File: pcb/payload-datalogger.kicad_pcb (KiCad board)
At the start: 2 copper layers, 43.5 x 41 mm, 42 parts, among them J1 2.54mm 01x02 header, J2 Conn_01x02, J3 Conn_01x02, J4 Conn_01x02, J5 Conn_01x02, SW2 PTS815, U1 XIAO-ESP32-C3-DIP, U2 NCP177AMX330TCG, U3 W25X40CLSN, U4 MCP96RL00T-E_MX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

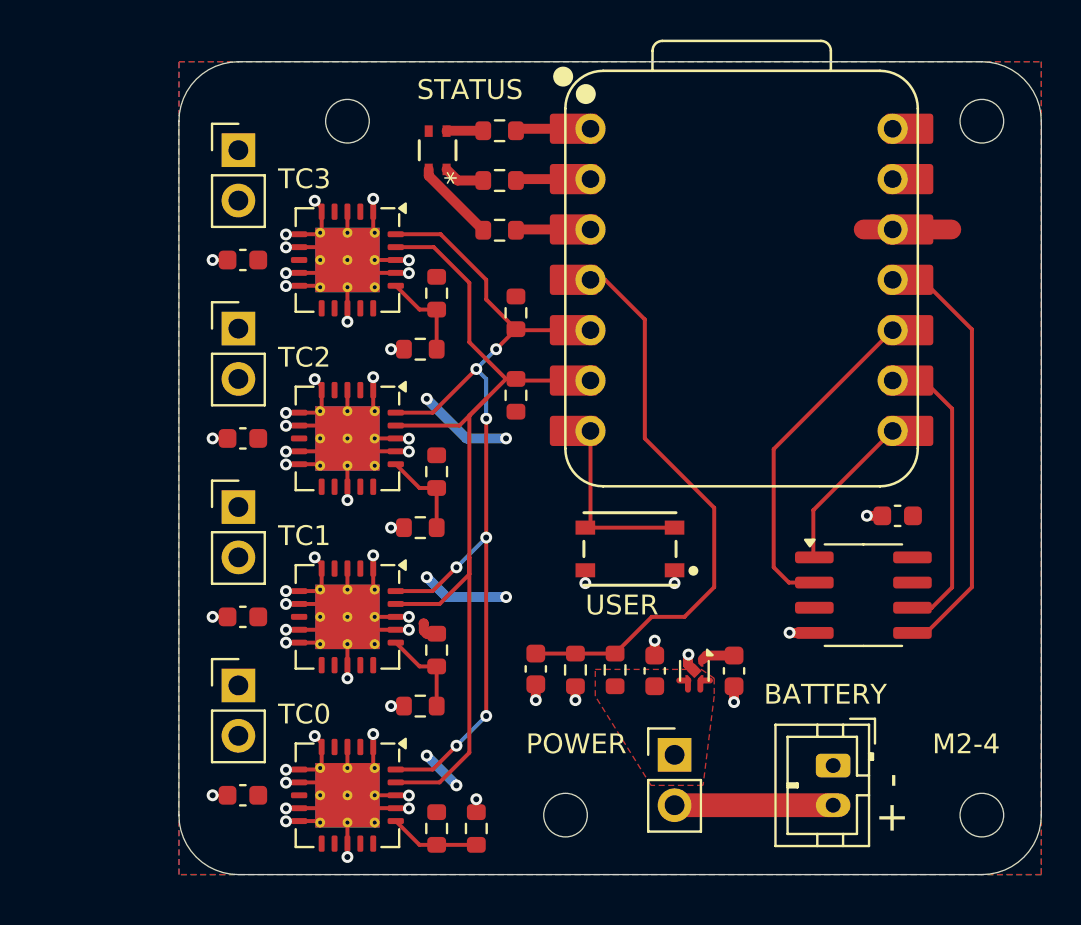
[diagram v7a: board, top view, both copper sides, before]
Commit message: Update PCB to use d sub
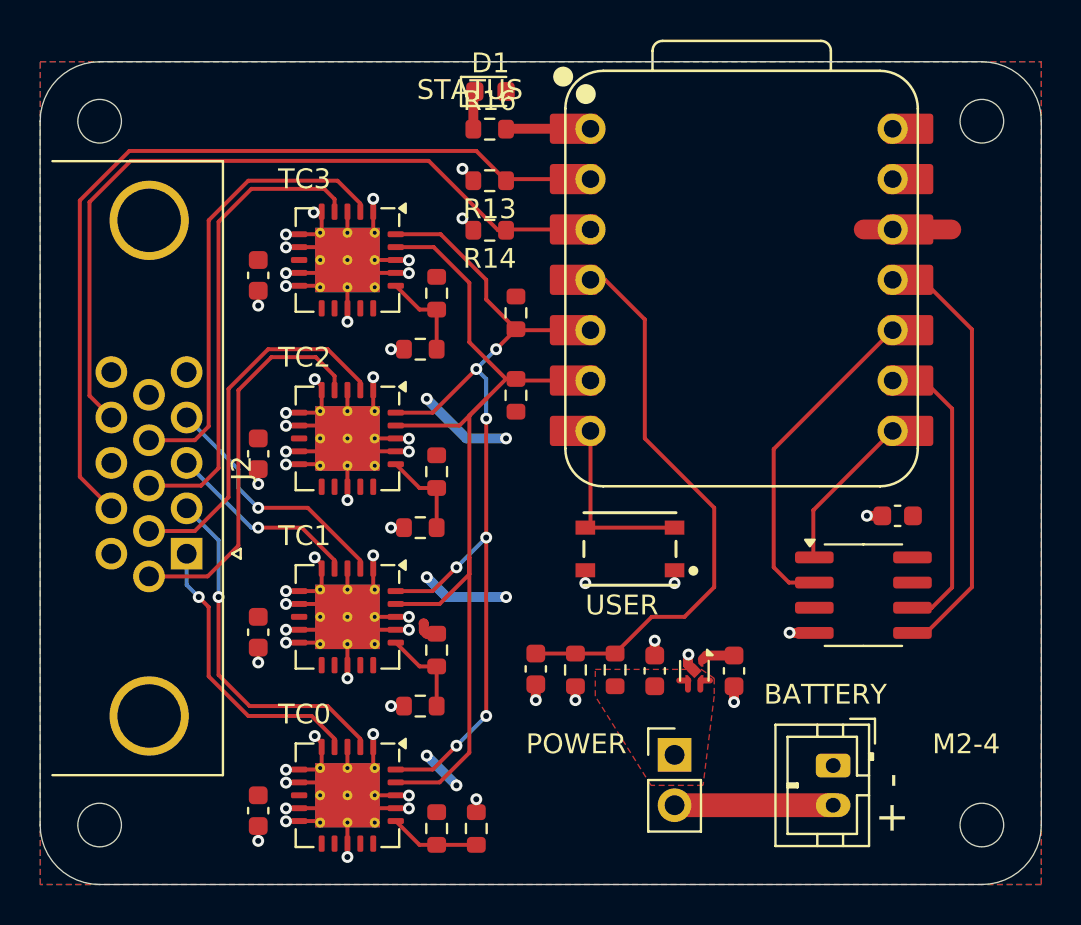
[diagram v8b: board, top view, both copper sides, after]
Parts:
- removed D2: B38G3RGB, B38G3RGB:B38G3RGB-10D0003H2U1930_HVK
- removed J3, J4, J5: Conn_01x02, Connector_PinHeader_2.54mm:PinHeader_1x02_P2.54mm_Vertical
- removed R15: 62, Resistor_SMD:R_0603_1608Metric
- added D1: B1911USD, LED_SMD:LED_0603_1608Metric, F.Cu at (87.2, 40.5)
- added R16: 270, Resistor_SMD:R_0603_1608Metric, F.Cu at (87.2, 42.4)
- J2: value Conn_01x02 -> DE15 Socket; footprint Connector_PinHeader_2.54mm:PinHeader_1x02_P2.54mm_Vertical -> Connector_Dsub:DSUB-15-HD_Socket_Horizontal_P2.29x1.90mm_EdgePinOffset3.03mm_Housed_MountingHolesOffset4.94mm
- R13: value 261 -> 10k
- R14: value 62 -> 10k
- moved REF** 23.5 mm to (67.5, 77.5)
- moved REF** 12.5 mm to (67.5, 42.0)
- moved J2 7.14 mm to (71.9, 63.8), turned to -90 degrees
- moved R13 2.57 mm to (87.2, 45.0), turned to 180 degrees
- moved R14 2.56 mm to (87.2, 47.5), turned to 180 degrees
- moved C5 1.10 mm to (75.5, 76.8), turned to -90 degrees
- moved C6 1.10 mm to (75.5, 67.8), turned to -90 degrees
- moved C7 1.10 mm to (75.5, 58.8), turned to -90 degrees
- moved C8 1.10 mm to (75.5, 49.8), turned to -90 degrees
- moved REF** 0.50 mm to (112.0, 77.5)
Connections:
- J2 pad 1: Net-(J2-Pin_1) -> /TC0-
- J2 pad 2: Net-(J2-Pin_2) -> /TC0+
- R13 pad 1: Net-(D2-RK) -> /NTC0-
- R13 pad 2: /LED_R -> GND
- R14 pad 1: Net-(D2-GK) -> /NTC1-
- R14 pad 2: /LED_G -> GND
- U1 pad 1: /LED_R -> Net-(U1-GPIO2/A0/D0)
- U1 pad 2: /LED_G -> /NTC0-
- U1 pad 3: /LED_B -> /NTC1-
- U4 pad 2: Net-(J2-Pin_1) -> /TC0+
- U4 pad 4: Net-(J2-Pin_2) -> /TC0-
- U5 pad 2: Net-(J3-Pin_1) -> /TC1+
- U5 pad 4: Net-(J3-Pin_2) -> /TC1-
- U6 pad 2: Net-(J4-Pin_1) -> /TC2+
- U6 pad 4: Net-(J4-Pin_2) -> /TC2-
- U7 pad 2: Net-(J5-Pin_1) -> /TC3+
- U7 pad 4: Net-(J5-Pin_2) -> /TC3-
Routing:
- net /NTC0-: track 0.00 -> 42.8 mm
- net /NTC1-: track 0.00 -> 38.1 mm
- net /TC3-: track 0.00 -> 23.7 mm
- net /TC3+: track 0.00 -> 23.1 mm
- net /TC2-: track 0.00 -> 19.6 mm
- net /TC2+: track 0.00 -> 18.8 mm
- net /TC0+: track 0.00 -> 18.0 mm, vias 0 -> 1
- net /TC0-: track 0.00 -> 14.7 mm, vias 0 -> 1
- net /TC1+: track 0.00 -> 12.7 mm, vias 0 -> 1
- net /TC1-: track 0.00 -> 9.91 mm, vias 0 -> 1
- net Net-(D2-BK): track 4.21 -> 0.00 mm
- net Net-(U1-GPIO2/A0/D0): track 0.00 -> 3.43 mm
- net /LED_R: track 2.97 -> 0.00 mm
- net /LED_G: track 2.95 -> 0.00 mm
- net /LED_B: track 2.94 -> 0.00 mm
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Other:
- board size 43.5 x 41 mm -> 50.5 x 41.5 mm
